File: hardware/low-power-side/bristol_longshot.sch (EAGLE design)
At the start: 73 parts, among them U1 SAM_D20E, U10 ADP1607ACPZN-R7, U11 TPS73118DBVT, U12 LIS2DH, U2 SI4060, U3 SE880, U4 SST25WF040BT-40I/NP, U5 TG-5006CJ, U6 TG-5006CJ, U7 TPS3123, U8 SN74LVC1G32DCKR, U9 MS5607-02BA03, Y1 ABS05

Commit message: [low-power-side] v0.986.5 Added TS3006 low power clock
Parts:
- removed C7: 15pF, microbuilder_v3:CAP_CERAMIC_0402
- added R12: 4.32MΩ, microbuilder_v3:RESISTOR_0402
- added U13: TS3006, TS3006:TS3006
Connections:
- new net LF_CLOCK: U1.PA27, U13.FOUT
- new net LF_RSET: R12.2, U13.RSET
- net 1.8V: now also U13.VDD
- net GND: now also R12.1, U13.GND, U13.GND1, U13.GND2, U13.GND3, U13.GND4; no longer C7.P$2
- net RADIO_VDD: no longer C7.P$1
- net SI_GPIO0: no longer U1.PA27
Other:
- note added: "(GCLK_IO[0])"
- note added: "Rset = 4.32MΩ for 25kHz output"
- note added: "TS3006 Low frequency clock"
- note removed: "Internal pull-up"
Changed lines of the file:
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@@
 <part name="C8" library="microbuilder_v3" deviceset="CAP_CERAMIC" device="_0402" value="100pF"/>
 <part name="U$57" library="microbuilder_v3" deviceset="GND" device=""/>
-<part name="C7" library="microbuilder_v3" deviceset="CAP_CERAMIC" device="_0402" value="15pF"/>
-<part name="U$58" library="microbuilder_v3" deviceset="GND" device=""/>
 <part name="C9" library="microbuilder_v3" deviceset="CAP_CERAMIC" device="_0402" value="100pF"/>
 <part name="U$3" library="microbuilder_v3" deviceset="GND" device=""/>
@@
 <part name="U$66" library="microbuilder_v3" deviceset="1.8V" device=""/>
 <part name="U$69" library="microbuilder_v3" deviceset="1.8V" device=""/>
+<part name="U13" library="TS3006" deviceset="TS3006" device=""/>
+<part name="U$72" library="microbuilder_v3" deviceset="GND" device=""/>
+<part name="U$74" library="microbuilder_v3" deviceset="GND" device=""/>
+<part name="U$76" library="microbuilder_v3" deviceset="GND" device=""/>
+<part name="U$77" library="microbuilder_v3" deviceset="GND" device=""/>
+<part name="U$80" library="microbuilder_v3" deviceset="GND" device=""/>
+<part name="R12" library="microbuilder_v3" deviceset="RESISTOR" device="_0402" value="4.32MΩ"/>
+<part name="U$81" library="microbuilder_v3" deviceset="GND" device=""/>
+<part name="U$82" library="microbuilder_v3" deviceset="1.8V" device=""/>
 </parts>
 <sheets>
@@
 <wire x1="489.204" y1="62.484" x2="489.204" y2="60.452" width="0.1524" layer="97"/>
 <wire x1="555.244" y1="72.644" x2="555.244" y2="68.072" width="0.1524" layer="97"/>
-<text x="109.22" y="139.954" size="1.27" layer="97" font="vector" ratio="11" rot="MR0">Internal pull-up</text>
 <text x="83.82" y="137.668" size="1.27" layer="97" font="vector" ratio="11">(AIN[0])</text>
 <wire x1="456.184" y1="57.404" x2="456.184" y2="52.832" width="0.1524" layer="97"/>
@@
 Specified 1.76V - 1.85V</text>
 <text x="281.94" y="99.06" size="2.54" layer="97" font="vector" ratio="11">LIS2D 3-axis accelerometer</text>
+<text x="190.5" y="122.428" size="1.27" layer="97" font="vector" ratio="11">(GCLK_IO[0])</text>
+<text x="287.02" y="175.26" size="2.54" layer="97" font="vector" ratio="11">TS3006 Low frequency clock</text>
+<text x="332.74" y="145.288" size="1.27" layer="97" font="vector" ratio="11" distance="100">Rset = 4.32MΩ
+for 25kHz output</text>
 </plain>
 <instances>
@@
 <instance part="C8" gate="G$1" x="571.5" y="208.28"/>
 <instance part="U$57" gate="G$1" x="571.5" y="203.2"/>
-<instance part="C7" gate="G$1" x="581.66" y="208.28"/>
-<instance part="U$58" gate="G$1" x="581.66" y="203.2"/>
 <instance part="C9" gate="G$1" x="462.28" y="96.52"/>
 <instance part="U$3" gate="G$1" x="462.28" y="88.9"/>
@@
 <instance part="U$66" gate="G$1" x="314.96" y="88.9" rot="MR0"/>
 <instance part="U$69" gate="G$1" x="292.1" y="55.88" rot="MR270"/>
+<instance part="U13" gate="G$1" x="304.8" y="149.86"/>
+<instance part="U$72" gate="G$1" x="299.72" y="132.08"/>
+<instance part="U$74" gate="G$1" x="302.26" y="132.08"/>
+<instance part="U$76" gate="G$1" x="304.8" y="132.08"/>
+<instance part="U$77" gate="G$1" x="307.34" y="132.08"/>
+<instance part="U$80" gate="G$1" x="309.88" y="132.08"/>
+<instance part="R12" gate="G$1" x="327.66" y="139.7" rot="R90"/>
+<instance part="U$81" gate="G$1" x="327.66" y="132.08"/>
+<instance part="U$82" gate="G$1" x="287.02" y="165.1" rot="MR0"/>
 </instances>
 <busses>
@@
 </segment>
 <segment>
-<pinref part="C7" gate="G$1" pin="P$2"/>
-<pinref part="U$58" gate="G$1" pin="GND"/>
-</segment>
-<segment>
 <pinref part="C9" gate="G$1" pin="P$2"/>
 <pinref part="U$3" gate="G$1" pin="GND"/>
@@
 <pinref part="U12" gate="G$1" pin="GND2"/>
 <pinref part="GND5" gate="1" pin="GND"/>
+</segment>
+<segment>
+<pinref part="U13" gate="G$1" pin="GND"/>
+<pinref part="U$72" gate="G$1" pin="GND"/>
+</segment>
+<segment>
+<pinref part="U13" gate="G$1" pin="GND1"/>
+<pinref part="U$74" gate="G$1" pin="GND"/>
+</segment>
+<segment>
+<pinref part="U13" gate="G$1" pin="GND2"/>
+<pinref part="U$76" gate="G$1" pin="GND"/>
+</segment>
+<segment>
+<pinref part="U13" gate="G$1" pin="GND3"/>
+<pinref part="U$77" gate="G$1" pin="GND"/>
+</segment>
+<segment>
+<pinref part="U13" gate="G$1" pin="GND4"/>
+<pinref part="U$80" gate="G$1" pin="GND"/>
+</segment>
+<segment>
+<pinref part="R12" gate="G$1" pin="1"/>
+<pinref part="U$81" gate="G$1" pin="GND"/>
 </segment>
 </net>
@@
 <junction x="297.18" y="55.88"/>
 </segment>
+<segment>
+<pinref part="U$82" gate="G$1" pin="1.8V"/>
+<wire x1="287.02" y1="162.56" x2="287.02" y2="157.48" width="0.1524" layer="91"/>
+<pinref part="U13" gate="G$1" pin="VDD"/>
+<wire x1="287.02" y1="157.48" x2="289.56" y2="157.48" width="0.1524" layer="91"/>
+</segment>
 </net>
 <net name="VDD_CORE" class="0">
@@
 <wire x1="632.46" y1="185.42" x2="650.24" y2="185.42" width="0.1524" layer="91"/>
 <label x="635" y="185.42" size="1.778" layer="95" ratio="11"/>
-</segment>
-<segment>
-<pinref part="U1" gate="G$1" pin="PA27"/>
-<wire x1="167.64" y1="121.92" x2="182.88" y2="121.92" width="0.1524" layer="91"/>
-<label x="170.18" y="121.92" size="1.778" layer="95" ratio="11"/>
 </segment>
 </net>
@@
 <pinref part="C25" gate="G$1" pin="P$1"/>
 <wire x1="561.34" y1="215.9" x2="571.5" y2="215.9" width="0.1524" layer="91"/>
-<wire x1="571.5" y1="215.9" x2="581.66" y2="215.9" width="0.1524" layer="91"/>
-<wire x1="581.66" y1="215.9" x2="594.36" y2="215.9" width="0.1524" layer="91"/>
+<wire x1="571.5" y1="215.9" x2="594.36" y2="215.9" width="0.1524" layer="91"/>
 <wire x1="551.18" y1="215.9" x2="551.18" y2="213.36" width="0.1524" layer="91"/>
 <pinref part="C20" gate="G$1" pin="P$1"/>
@@
 <pinref part="C8" gate="G$1" pin="P$1"/>
 <wire x1="571.5" y1="215.9" x2="571.5" y2="213.36" width="0.1524" layer="91"/>
-<pinref part="C7" gate="G$1" pin="P$1"/>
-<wire x1="581.66" y1="215.9" x2="581.66" y2="213.36" width="0.1524" layer="91"/>
 <junction x="561.34" y="215.9"/>
 <junction x="571.5" y="215.9"/>
-<junction x="581.66" y="215.9"/>
 </segment>
 </net>
@@
 </segment>
 </net>
+<net name="LF_RSET" class="0">
+<segment>
+<pinref part="U13" gate="G$1" pin="RSET"/>
+<pinref part="R12" gate="G$1" pin="2"/>
+<wire x1="320.04" y1="149.86" x2="327.66" y2="149.86" width="0.1524" layer="91"/>
+<wire x1="327.66" y1="149.86" x2="327.66" y2="144.78" width="0.1524" layer="91"/>
+</segment>
+</net>
+<net name="LF_CLOCK" class="0">
+<segment>
+<pinref part="U13" gate="G$1" pin="FOUT"/>
+<wire x1="320.04" y1="157.48" x2="350.52" y2="157.48" width="0.1524" layer="91"/>
+<label x="325.12" y="157.48" size="1.778" layer="95"/>
+</segment>
+<segment>
+<pinref part="U1" gate="G$1" pin="PA27"/>
+<wire x1="167.64" y1="121.92" x2="187.96" y2="121.92" width="0.1524" layer="91"/>
+<label x="172.72" y="121.92" size="1.778" layer="95"/>
+</segment>
+</net>

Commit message: [low power] v0.986.6. Added LDO for GPS, LF TCXO for GPS
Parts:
- removed FB3: (no value), microbuilder_v3:FERRITE_0402
- removed Y1: ABS05, fbri:ABS05
- added JP1: (no value), SparkFun:M02LOCK
- added R13: 10kΩ, microbuilder_v3:RESISTOR_0402
- added U14: SIT1552, fbri:SIT1552
- added U15: LIS2DH, fbri:LIS2DH
- C11: value 1nF -> 10nF
- C27: value 18pF -> 1nF
- C28: value 18pF -> 1µF
- U12: value LIS2DH -> TPS73118DBVT; device fbri:LIS2DH -> TPS73118DVBT:TPS73118DBVT
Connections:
- new net BOOST_EN: JP1.2, R13.1, U10.EN
- new net GPS_REG_NR: C11.P$1, U12.NR/FB
- net !RESET: now also U12.EN
- net 1.2V: now also R13.2; no longer U10.EN
- net 1.8V: now also C14.P$1, U12.IN, U15.CS, U15.SDO/SA0, U15.VDD, U15.VDD_IO; no longer FB3.P$2, U12.CS, U12.SDO/SA0, U12.VDD, U12.VDD_IO
- net GND: now also JP1.1, U14.GND, U14.GND1, U15.GND, U15.GND1, U15.GND2; no longer U12.GND1, U12.GND2
- net GPS_VDD: now also C28.P$1, U12.OUT, U14.VCC; no longer C14.P$1, FB3.P$1
- net RTC_XI: now also U14.OUT; no longer C27.P$1, Y1.1
- net RTC_XO: no longer C28.P$1, Y1.2
- net SCL: now also U15.SCL/SPC; no longer U12.SCL/SPC
- net SDA: now also U15.SDA/SDI/SDO; no longer U12.SDA/SDI/SDO
- net TCXO_VDD1: now also C27.P$1; no longer C11.P$1
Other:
- note added: "180ms low on reset"
- note added: "Bypass Capacitors near SE880 main feed"
- note added: "Regulator included to cycle power on failure, also for power conditioning"
- note added: "Startup within 300ms"
- note removed: "Not used"
- moved on the sheet: C11, C14, C22, C27, C28, C31, C9, L1, L8, L9, R2, R3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

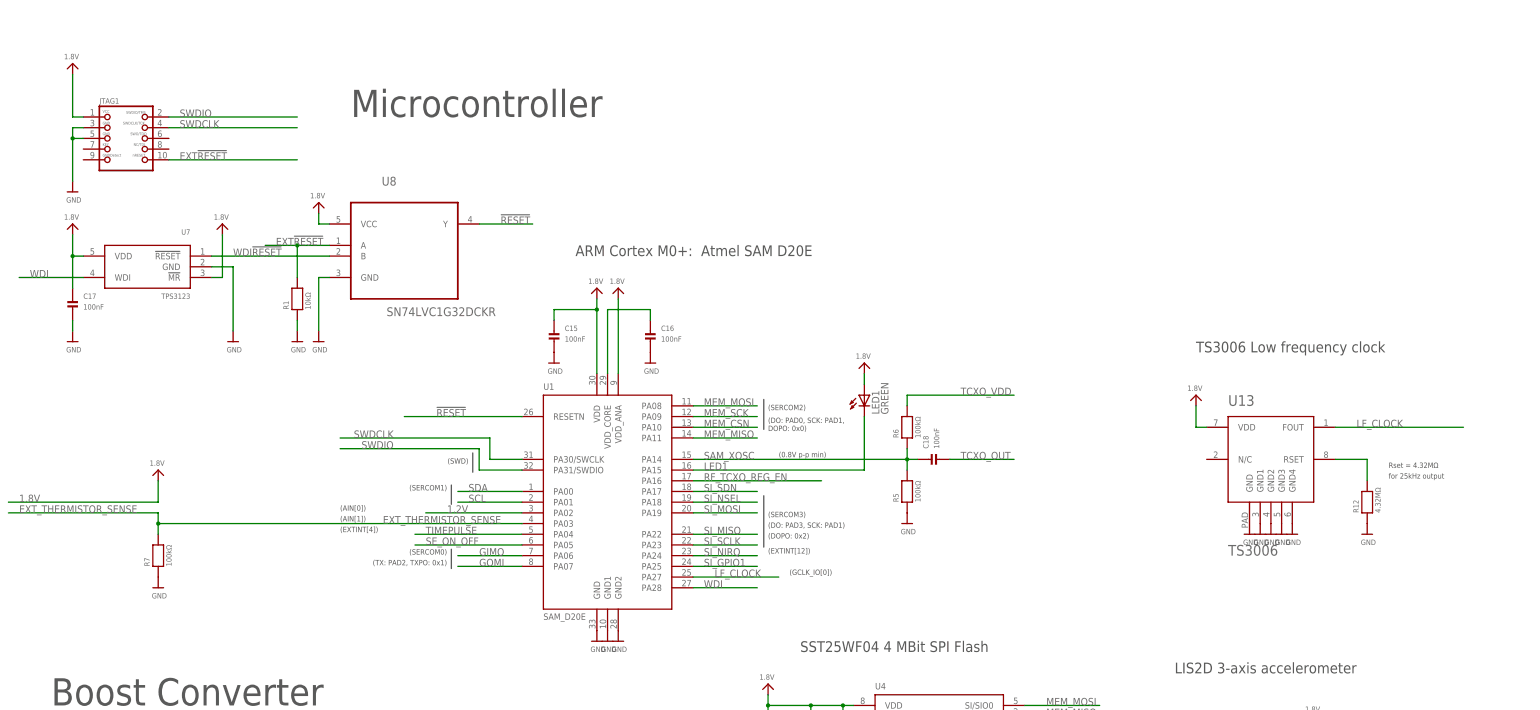
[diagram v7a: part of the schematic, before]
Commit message: [low power] v0.986.7. Changed low power lf clock, added vreg on breakout for optional power testing
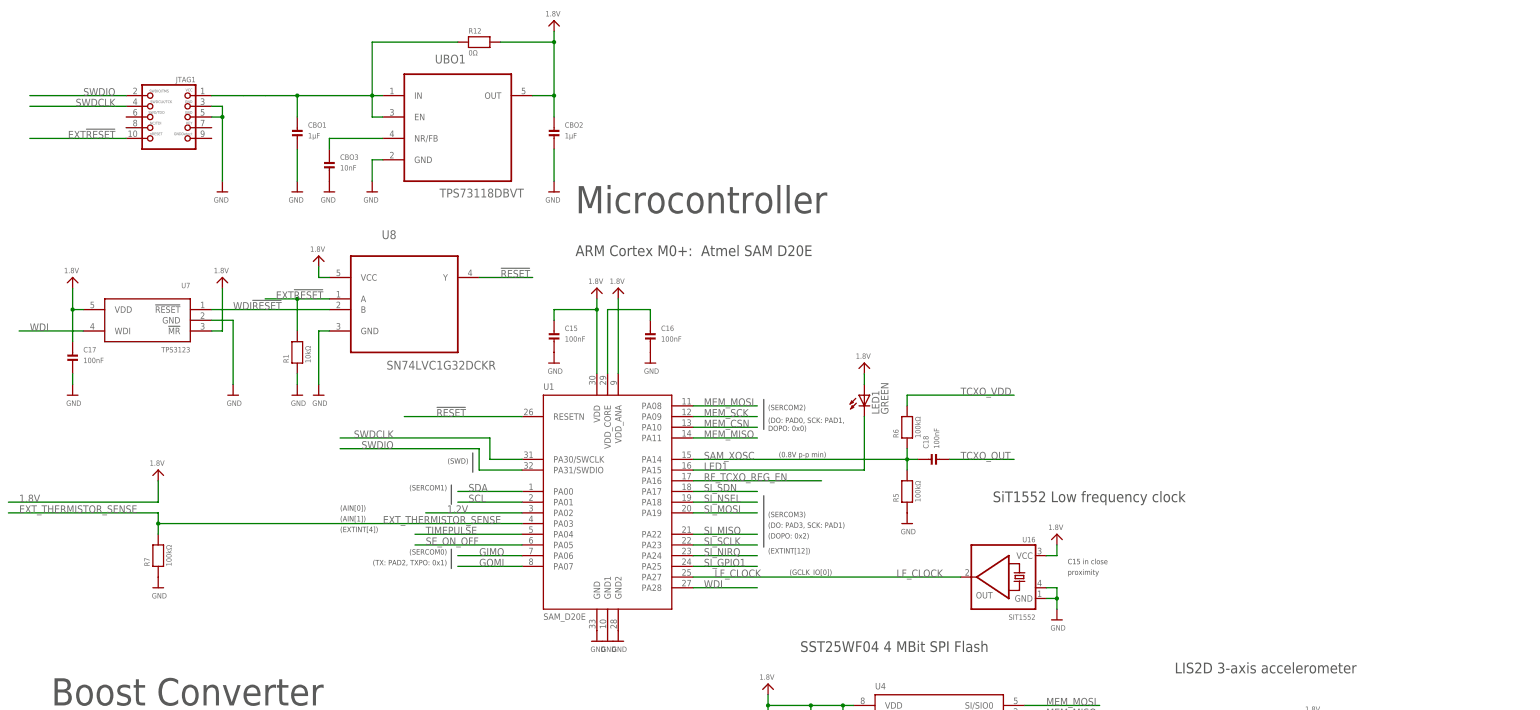
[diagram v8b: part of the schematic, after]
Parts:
- removed U13: TS3006, TS3006:TS3006
- added CBO1, CBO2: 1µF, microbuilder_v3:CAP_CERAMIC_0402
- added CBO3: 10nF, microbuilder_v3:CAP_CERAMIC_0402
- added U16: SIT1552, fbri:SIT1552
- added UBO1: TPS73118DBVT, TPS73118DVBT:TPS73118DBVT
- R12: value 4.32MΩ -> 0Ω
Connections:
- removed net LF_RSET: R12.2, U13.RSET
- new net JTAG_VIN: CBO1.P$1, JTAG1.1, R12.1, UBO1.EN, UBO1.IN
- new net JTAG_VREG_NR: CBO3.P$1, UBO1.NR/FB
- net 1.8V: now also CBO2.P$1, R12.2, U16.VCC, UBO1.OUT; no longer JTAG1.1, U13.VDD
- net GND: now also CBO1.P$2, CBO2.P$2, CBO3.P$2, U16.GND, U16.GND1, UBO1.GND; no longer R12.1, U13.GND, U13.GND1, U13.GND2, U13.GND3, U13.GND4
- net LF_CLOCK: now also U16.OUT; no longer U13.FOUT
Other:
- note added: "C15 in close proximity"
- note added: "SiT1552 Low frequency clock"
- note removed: "Rset = 4.32MΩ for 25kHz output"
- note removed: "TS3006 Low frequency clock"
- moved on the sheet: C17, JTAG1, R1, R12, U7, U8
